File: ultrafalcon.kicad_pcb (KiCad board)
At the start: 2 copper layers, 78 x 78 mm, 44 parts, among them J1 Conn_01x08_Socket, SW1 RotaryEncoder, SW2 SW_Push, U1 SK6805-EC15, U10 SK6805-EC15, U11 SK6805-EC15, U12 SK6805-EC15, U13 SK6805-EC15, U14 SK6805-EC15, U15 SK6805-EC15, U16 SK6805-EC15, U17 SK6805-EC15, U18 SK6805-EC15, U19 SK6805-EC15, U2 SK6805-EC15, U20 SK6805-EC15, U21 SK6805-EC15, U22 SK6805-EC15, U23 SK6805-EC15, U24 SK6805-EC15, U25 SK6805-EC15, U26 SK6805-EC15, U27 SK6805-EC15, U28 SK6805-EC15, U29 SK6805-EC15, U3 SK6805-EC15, U30 SK6805-EC15, U4 SK6805-EC15, U5 SK6805-EC15, U6 SK6805-EC15, U7 SK6805-EC15, U8 SK6805-EC15, U9 SK6805-EC15

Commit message: getting the board ready for pcbway
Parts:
- C1, C2: value CL05B104KO5NNNC -> 0.01uF
- R2, R3, R4, R5: value 0603WAF3300T5E -> 10k
- SW1: value RotaryEncoder -> PER601-P117-N0015
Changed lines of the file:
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@@
         (effects (font (size 1 1) (thickness 0.15)))
     )
-    (fp_text value "0603WAF3300T5E" (at 0 2.660605 90) (layer "F.Fab") hide
+    (fp_text value "10k" (at 0 2.660605 90) (layer "F.Fab") hide
         (effects (font (size 1 1) (thickness 0.15)))
     )
@@
         (effects (font (size 1 1) (thickness 0.15)))
     )
-    (fp_text value "0603WAF3300T5E" (at 0 2.660605 90) (layer "F.Fab") hide
+    (fp_text value "10k" (at 0 2.660605 90) (layer "F.Fab") hide
         (effects (font (size 1 1) (thickness 0.15)))
     )
@@
         (effects (font (size 1 1) (thickness 0.15)))
     )
-    (fp_text value "CL05B104KO5NNNC" (at 0 2.498603 90) (layer "F.Fab") hide
+    (fp_text value "0.01uF" (at 0 2.498603 90) (layer "F.Fab") hide
         (effects (font (size 1 1) (thickness 0.15)))
     )
@@
         (effects (font (size 1 1) (thickness 0.15)))
     )
-    (fp_text value "RotaryEncoder" (at 0 0) (layer "F.Fab")
+    (fp_text value "PER601-P117-N0015" (at 0 0) (layer "F.Fab")
         (effects (font (size 1 1) (thickness 0.15)))
     )
@@
     (property "Sheetfile" "ultrafalcon.kicad_sch")
     (property "Sheetname" "")
+    (property "exclude_from_bom" "")
     (property "ki_description" "Push button switch, generic, two pins")
     (property "ki_keywords" "switch normally-open pushbutton push-button")
-    (attr through_hole)
+    (attr through_hole exclude_from_bom)
     (fp_text reference "SW2" (at 0 -8) (layer "F.SilkS") hide
         (effects (font (size 1 1) (thickness 0.15)))
@@
     (property "Sheetfile" "ultrafalcon.kicad_sch")
     (property "Sheetname" "")
+    (property "exclude_from_bom" "")
     (property "ki_description" "Mounting Hole without connection")
     (property "ki_keywords" "mounting hole")
-    (attr exclude_from_pos_files)
+    (attr exclude_from_pos_files exclude_from_bom)
     (fp_text reference "H1" (at 0 -4.2) (layer "F.SilkS") hide
         (effects (font (size 1 1) (thickness 0.15)))
@@
         (effects (font (size 1 1) (thickness 0.15)))
     )
-    (fp_text value "0603WAF3300T5E" (at 0 2.660605 90) (layer "F.Fab") hide
+    (fp_text value "10k" (at 0 2.660605 90) (layer "F.Fab") hide
         (effects (font (size 1 1) (thickness 0.15)))
     )
@@
         (effects (font (size 1 1) (thickness 0.15)))
     )
-    (fp_text value "CL05B104KO5NNNC" (at 0 2.498603 90) (layer "F.Fab") hide
+    (fp_text value "0.01uF" (at 0 2.498603 90) (layer "F.Fab") hide
         (effects (font (size 1 1) (thickness 0.15)))
     )
@@
         (effects (font (size 1 1) (thickness 0.15)))
     )
-    (fp_text value "0603WAF3300T5E" (at 0 2.660605 90) (layer "F.Fab") hide
+    (fp_text value "10k" (at 0 2.660605 90) (layer "F.Fab") hide
         (effects (font (size 1 1) (thickness 0.15)))
     )
@@
     (property "Sheetfile" "ultrafalcon.kicad_sch")
     (property "Sheetname" "")
+    (property "exclude_from_bom" "")
     (property "ki_description" "Mounting Hole without connection")
     (property "ki_keywords" "mounting hole")
-    (attr exclude_from_pos_files)
+    (attr exclude_from_pos_files exclude_from_bom)
     (fp_text reference "H2" (at 0 -4.2) (layer "F.SilkS") hide
         (effects (font (size 1 1) (thickness 0.15)))
@@
     (property "Sheetfile" "ultrafalcon.kicad_sch")
     (property "Sheetname" "")
+    (property "exclude_from_bom" "")
     (property "ki_description" "Generic connector, single row, 01x08, script generated")
     (property "ki_keywords" "connector")
-    (attr through_hole)
+    (attr through_hole exclude_from_bom)
     (fp_text reference "J1" (at 8.75 2.8 90) (layer "B.SilkS") hide
         (effects (font (size 1 1) (thickness 0.15)) (justify mirror))
@@
     (fp_line (start 20 1.6) (end -2.5 1.6)
       (stroke (width 0.1) (type solid)) (layer "B.Fab"))
-    (pad "1" thru_hole roundrect (at 0 0 90) (size 1.7 1.95) (drill 0.95) (layers "*.Cu" "*.Mask") (roundrect_rratio 0.147059)
+    (pad "1" thru_hole roundrect (at 0 0 90) (size 1.7 1.95) (drill 0.95) (layers "*.Cu" "*.Mask") (roundrect_rratio 0.1470588235)
       (net 2 "GND") (pinfunction "Pin_1") (pintype "passive"))
     (pad "2" thru_hole oval (at 2.5 0 90) (size 1.7 1.95) (drill 0.95) (layers "*.Cu" "*.Mask")

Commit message: jan22 updates, almost ready for production
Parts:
- added G***: LOGO, ct-kicad:pcbway-logo-neg40mm, B.Cu at (134.9, 117.6)
- added G***: LOGO, ct-kicad:ultrafalcon-qr-15mm, B.Cu at (150.0, 72.0)
- added J2: Conn_01x02_Socket, Connector_PinHeader_2.54mm:PinHeader_1x02_P2.54mm_Vertical, B.Cu at (140.4, 100.6)
- added LOGO2: **REF, ct-kicad:pcbway-logo-neg40mm, F.Cu at (20.0, 4.61)
- added LOGO3: **REF, ct-kicad:ultrafalcon-qr, F.Cu at (9.99, 21.1)
- C3: value CL05B104KO5NNNC -> 1uF
- R1: value 0603WAF3300T5E -> 330
- moved LOGO1 1.57 mm to (122.1, 90.5)
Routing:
- net SWITCH_A: track 0.00 -> 32.5 mm, vias 0 -> 3
- net SWITCH_B: track 0.00 -> 30.9 mm, vias 0 -> 3
- net GND: track 215.1 -> 219.4 mm
- net Net-(U1-DOUT): track 26.0 -> 26.9 mm
- net LED_DI: track 22.7 -> 23.4 mm

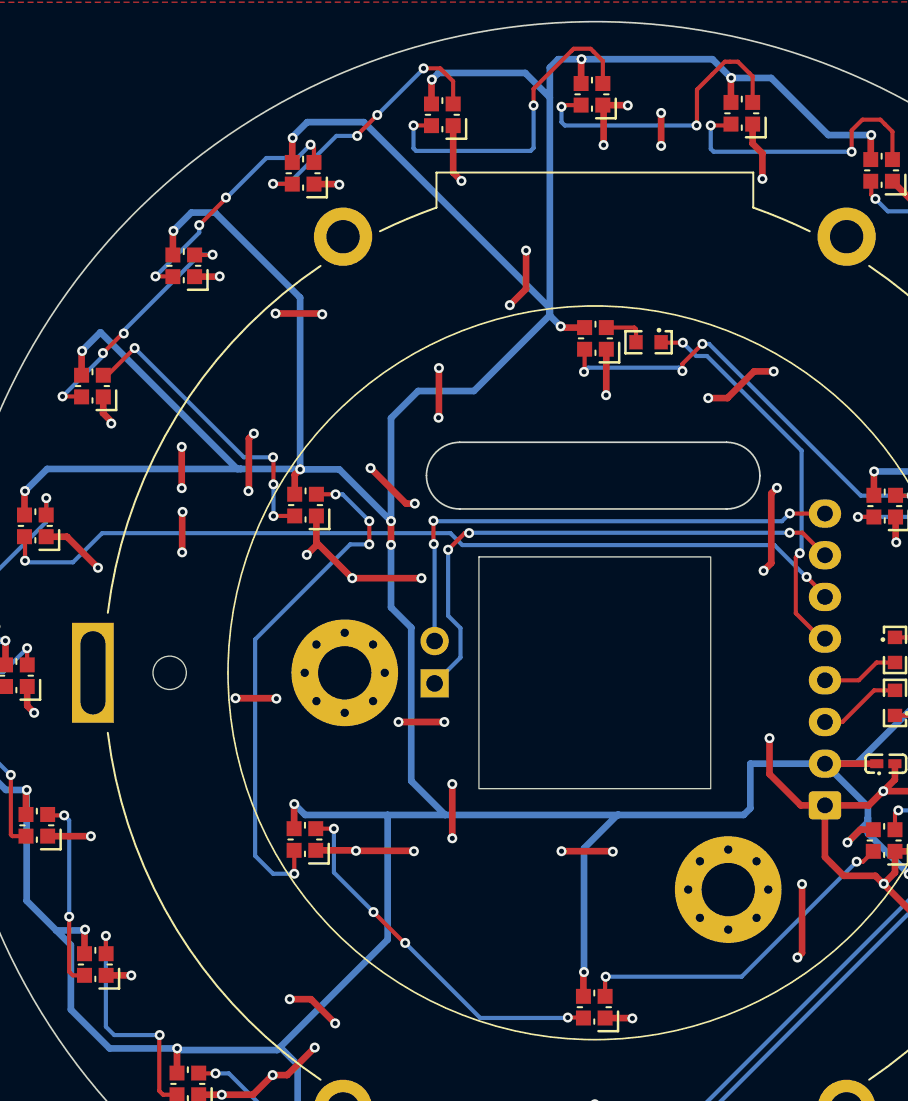
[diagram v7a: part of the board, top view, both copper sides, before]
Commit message: fixing some trace spacing
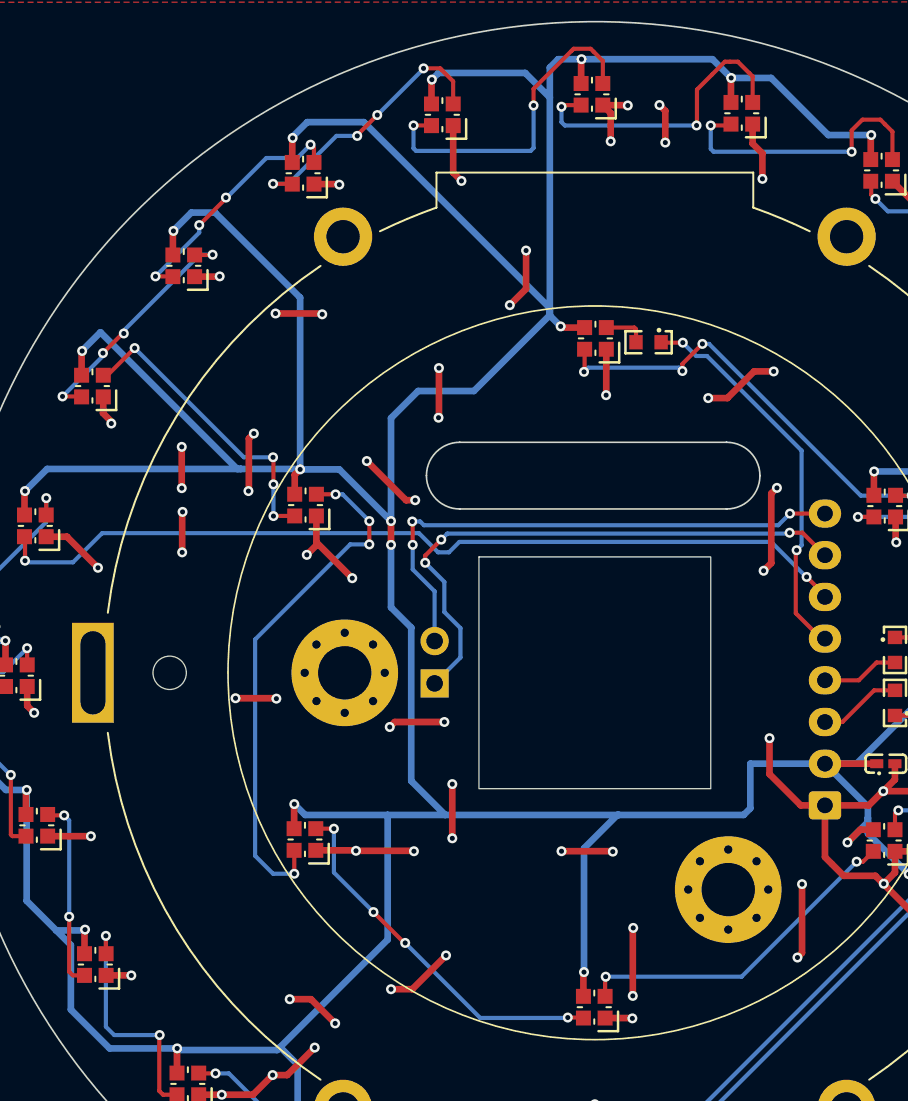
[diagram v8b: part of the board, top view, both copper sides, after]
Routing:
- net GND: track 219.4 -> 224.9 mm, vias 92 -> 95
- net SWITCH_B: track 30.9 -> 32.9 mm
- net SWITCH_A: track 32.5 -> 34.3 mm
- net LED_DO: track 51.8 -> 52.4 mm
